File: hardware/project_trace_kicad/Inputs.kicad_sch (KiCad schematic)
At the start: 46 parts, among them J102 Conn_Coaxial, J201 Conn_01x01_Socket, J202 Conn_01x01_Socket, J203 Conn_01x01_Socket, J204 Screw_Terminal_01x04, U101 AD8421, U102 AQW280SX, U201 AQW282SX, U202 DAC81401, U203 TS5A23159DGS, U204 ADA4807-2ACP

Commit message: Before Changes to Input Section
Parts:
- removed DZ201: WE-TVSP, Diode_SMD:D_SMC_Handsoldering, symbol PCM_Diode_Zener_AKL:D_Zener_Generic
- added C303: 100n, Capacitor_SMD:C_0603_1608Metric_Pad1.08x0.95mm_HandSolder, symbol Device:C
- added D201: SMAJ250A, Diode_SMD:D_SMA_Handsoldering, symbol Device:D_Zener_Filled
- added U302: ADA4807-4ARUZ, Package_SO:TSSOP-14_4.4x5mm_P0.65mm, symbol Amplifier_Operational:ADA4807-4ARUZ
- C201, C202, C204, C205, C206, C207: value 1u -> 100n; footprint (none) -> Capacitor_SMD:C_0603_1608Metric_Pad1.08x0.95mm_HandSolder
- C203, C?: footprint (none) -> Capacitor_SMD:C_0603_1608Metric_Pad1.08x0.95mm_HandSolder
- JP201, JP202, JP203, JP204, JP205: footprint (none) -> Jumper:SolderJumper-2_P1.3mm_Open_RoundedPad1.0x1.5mm
- U101: footprint Package_SO:SOIC-8_3.9x4.9mm_P1.27mm -> Package_SO:MSOP-8_3x3mm_P0.65mm; DigikeyPN (none) -> 505-AD8421ARMZ-RLCT-ND
- U203: DigikeyPN (none) -> 296-18598-1-ND
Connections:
- net +5V: now also C303.2, U302.4 (V+)
- net GND: now also DZ?.1 (K), J204.3 (Pin_3), R104.2, C303.1, D201.2 (A), U302.11 (V-); no longer R103.2
- net VCOM: now also R103.2; no longer DZ?.1 (K), J204.3 (Pin_3), R104.2
- net Voltmeter.In: now also D201.1 (K)
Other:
- note added: "1.8Vpp"
- note added: "5Vpp"
- note added: "TODO: Fix high relative uncertainty due to Ron"
- note added: "TODO: UPDATE AD4821 FOOTPRINT"
- note added: "TODO: Verify Footprint"
- note added: "TODO: use GND (Requires changes to R-LADDER)"
- note removed: "TODO: Use Diff-amp?"
- moved on the sheet: C204, R105, R?, U201B, U203C

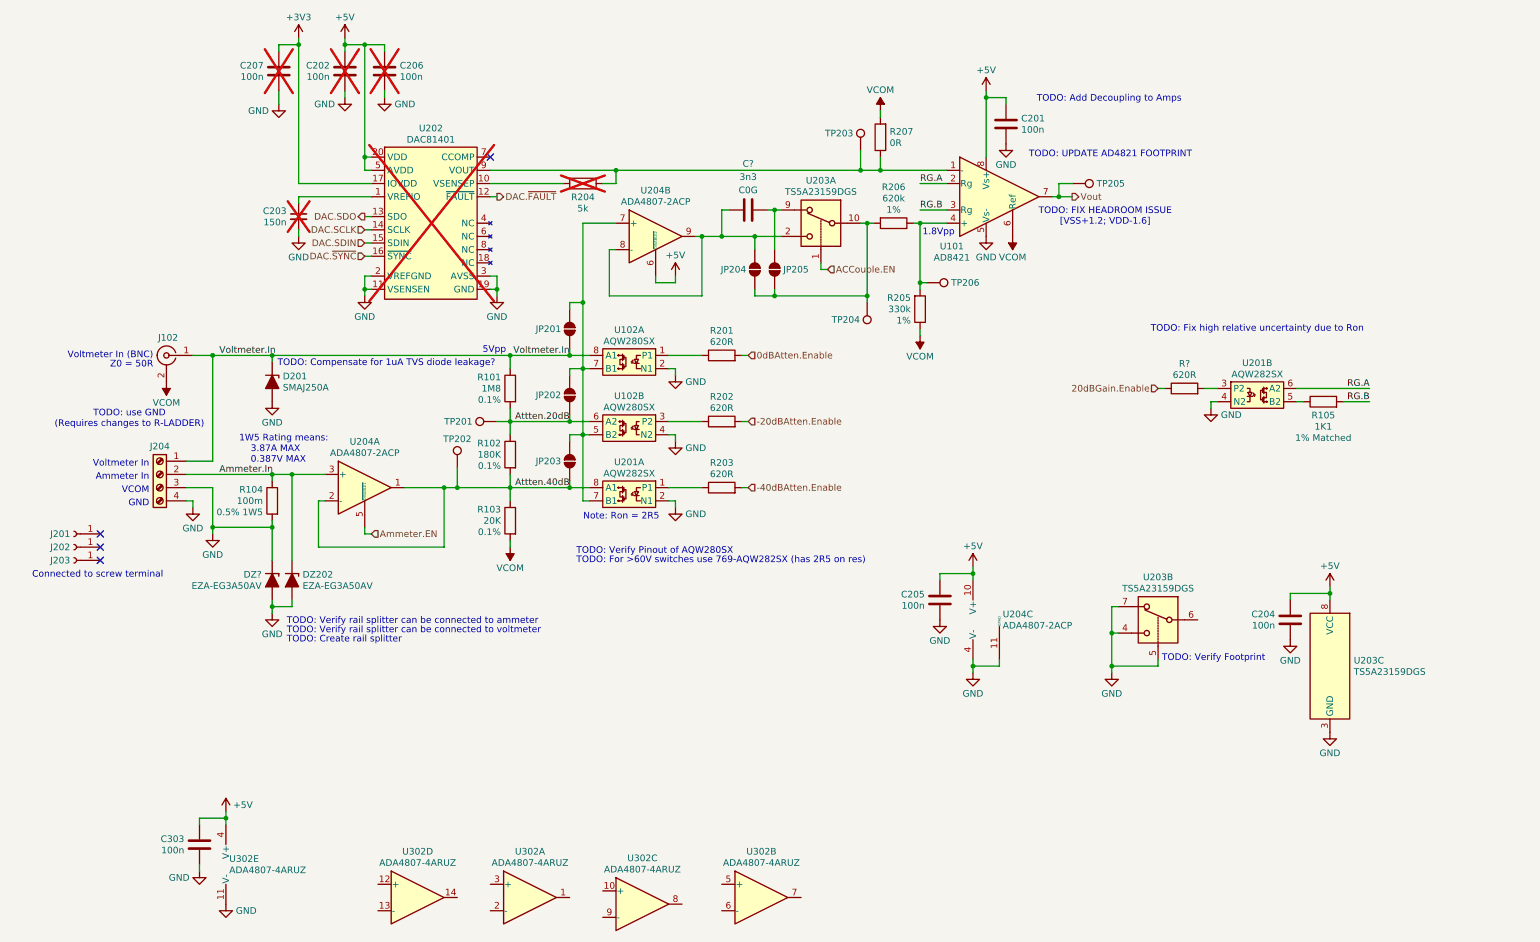
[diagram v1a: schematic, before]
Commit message: Add Pull-Up Network to Input
(Sync up laptop)
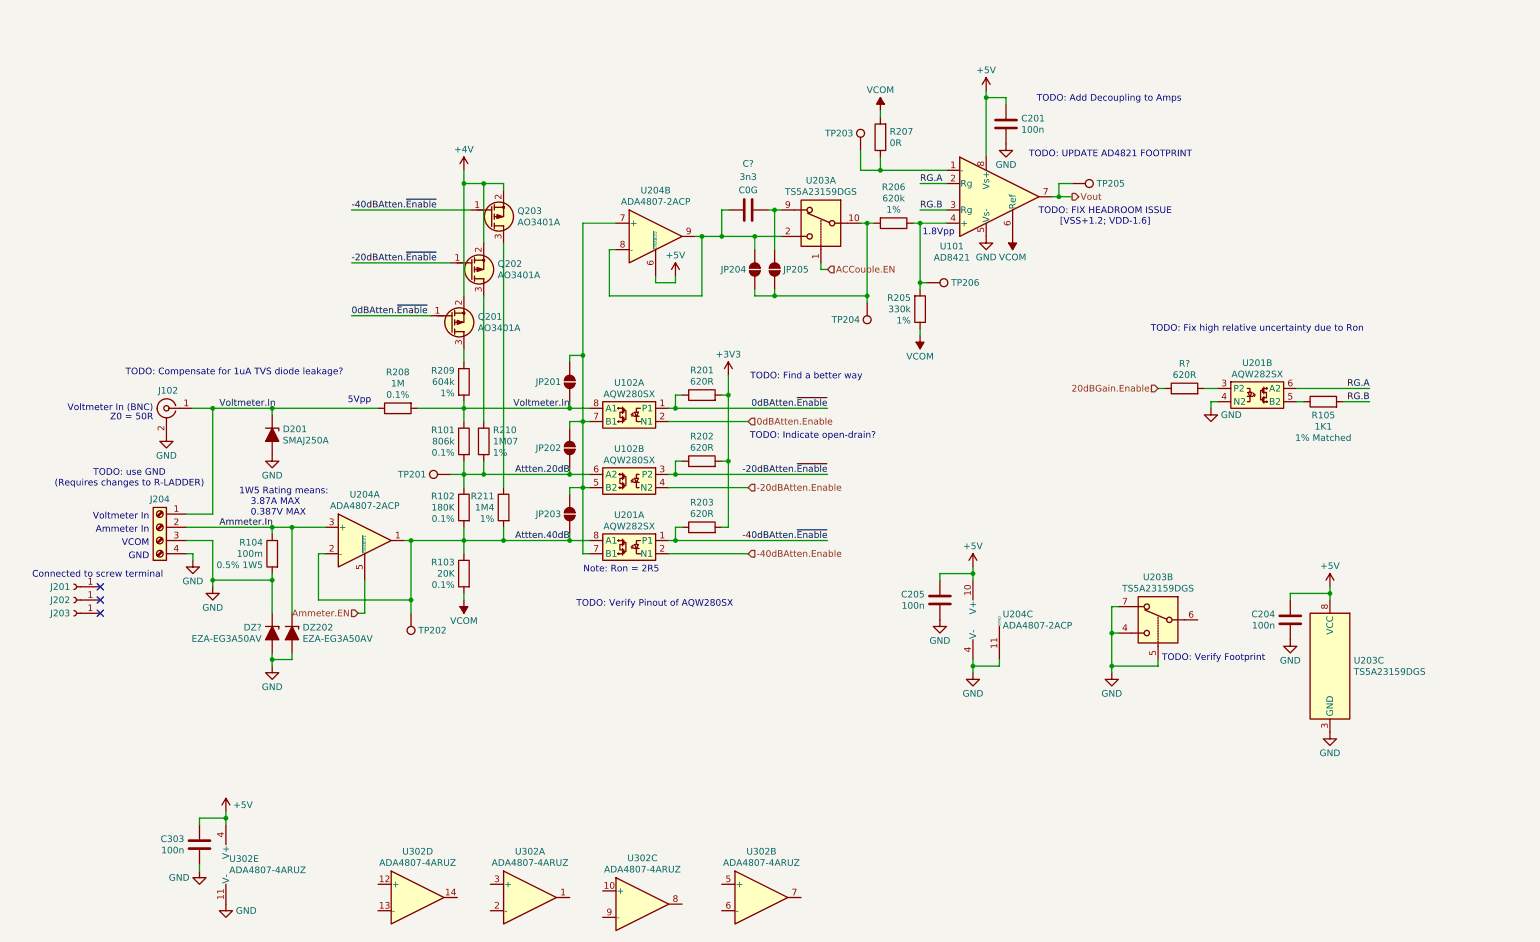
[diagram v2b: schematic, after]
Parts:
- removed C202, C206, C207: 100n, Capacitor_SMD:C_0603_1608Metric_Pad1.08x0.95mm_HandSolder, symbol Device:C
- removed C203: 150n, Capacitor_SMD:C_0603_1608Metric_Pad1.08x0.95mm_HandSolder, symbol Device:C_Small
- removed R204: 5k, symbol Device:R
- removed U202: DAC81401, Package_SO:Texas_PW0020A_TSSOP-20_4.4x6.5mm_P0.65mm, symbol ProjectTraceSymbols:DAC81401
- added Q201, Q202, Q203: AO3401A, PCM_Package_TO_SOT_SMD_AKL:SOT-23, symbol PCM_Transistor_MOSFET_AKL:AO3401A
- added R208: 1M, Resistor_SMD:R_0603_1608Metric_Pad0.98x0.95mm_HandSolder, symbol Device:R
- added R209: 604k, Resistor_SMD:R_0603_1608Metric_Pad0.98x0.95mm_HandSolder, symbol Device:R
- added R210: 1M07, Resistor_SMD:R_0603_1608Metric_Pad0.98x0.95mm_HandSolder, symbol Device:R
- added R211: 1M4, Resistor_SMD:R_0603_1608Metric_Pad0.98x0.95mm_HandSolder, symbol Device:R
- R101: value 1M8 -> 806k
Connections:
- net +3V3: now also R201.2, R202.2, R203.2
- net -20dBAtten.Enable: now also U102.4 (N2); no longer R202.2
- net -40dBAtten.Enable: now also U201.2 (N1); no longer R203.2
- net 0dBAtten.Enable: now also U102.2 (N1); no longer R201.2
- net Attten.20dB: now also R210.2
- net Attten.40dB: now also R211.2
- net GND: now also J102.2 (Ext); no longer U102.2 (N1), U102.4 (N2), U201.2 (N1)
- net VCOM: no longer J102.2 (Ext)
- net Voltmeter.In: now also R208.1, R208.2, R209.2
- net -40dBAtten.~{Enable}: now reaches R203.1, U201.1 (P1)
- net -40dBAtten.~{Enable}: now also Q203.1 (G)
- net 0dBAtten.~{Enable}: now reaches R201.1, U102.1 (P1)
- net 0dBAtten.~{Enable}: now also Q201.1 (G)
- net -20dBAtten.~{Enable}: now reaches R202.1, U102.3 (P2)
- net -20dBAtten.~{Enable}: now also Q202.1 (G)
- new net: Q201.3 (D), R209.1
- new net: Q202.3 (D), R210.1
- new net: Q203.3 (D), R211.1
- new net +4V: Q201.2 (S), Q202.2 (S), Q203.2 (S)
- no-connect marks 4 -> 3
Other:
- note added: "TODO: Find a better way"
- note added: "TODO: Indicate open-drain?"
- note removed: "TODO: Create rail splitter"
- note removed: "TODO: For >60V switches use 769-AQW282SX (has 2R5 on res)"
- note removed: "TODO: Verify rail splitter can be connected to ammeter"
- note removed: "TODO: Verify rail splitter can be connected to voltmeter"
- moved on the sheet: D201, DZ202, DZ?, J102, J201, J202, J203, J204, JP201, JP202, JP203, R101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

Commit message: Change designators, Improve Input Circuit
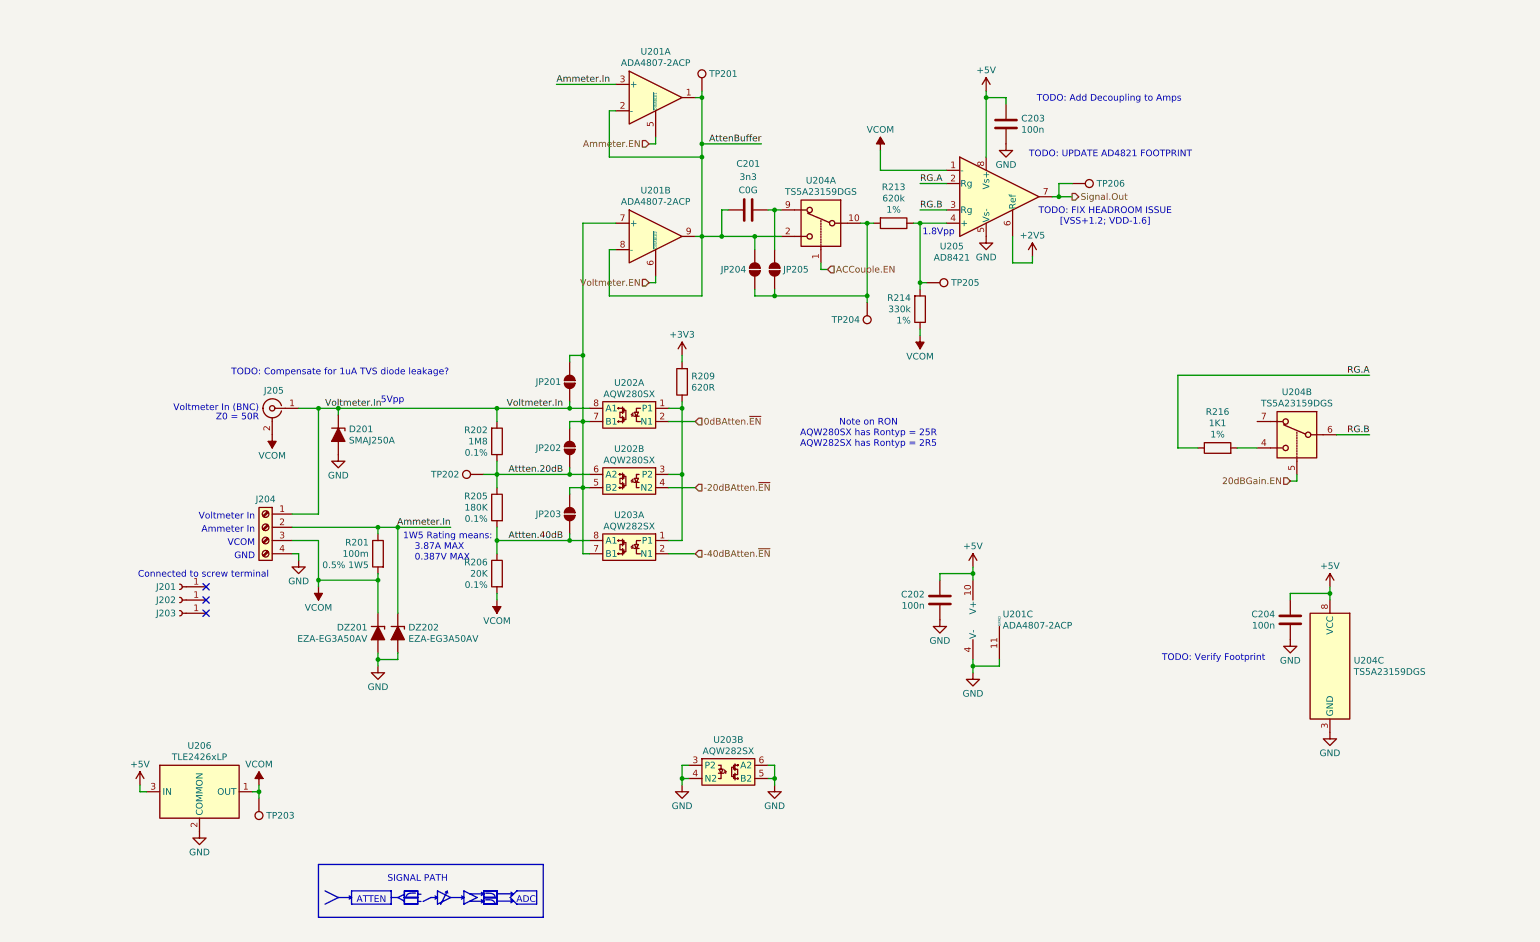
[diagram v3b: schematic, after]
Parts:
- removed C303: 100n, Capacitor_SMD:C_0603_1608Metric_Pad1.08x0.95mm_HandSolder, symbol Device:C
- removed Q201, Q202, Q203: AO3401A, PCM_Package_TO_SOT_SMD_AKL:SOT-23, symbol PCM_Transistor_MOSFET_AKL:AO3401A
- removed R101: 806k, Resistor_SMD:R_0603_1608Metric_Pad0.98x0.95mm_HandSolder, symbol Device:R
- removed R202, R203, R?: 620R, Resistor_SMD:R_0603_1608Metric_Pad0.98x0.95mm_HandSolder, symbol Device:R
- removed R207: 0R, symbol Device:R
- removed R209: 604k, Resistor_SMD:R_0603_1608Metric_Pad0.98x0.95mm_HandSolder, symbol Device:R
- removed R210: 1M07, Resistor_SMD:R_0603_1608Metric_Pad0.98x0.95mm_HandSolder, symbol Device:R
- removed R211: 1M4, Resistor_SMD:R_0603_1608Metric_Pad0.98x0.95mm_HandSolder, symbol Device:R
- removed U302: ADA4807-4ARUZ, Package_SO:TSSOP-14_4.4x5mm_P0.65mm, symbol Amplifier_Operational:ADA4807-4ARUZ
- added U206: TLE2426xLP, Package_TO_SOT_THT:TO-92_Inline_Wide, symbol Reference_Voltage:TLE2426xLP
- R202: renamed from R208; value 1M -> 1M8
- R216: renamed from R105; Extra 1% Matched -> 1%
- gave numbers to parts that had none: 2
- renumbered C205 to C202, C201 to C203, J102 to J205, R104 to R201, R102 to R205, R103 to R206, R201 to R209, R206 to R213, R205 to R214, TP202 to TP201, TP201 to TP202, TP206 to TP205, TP205 to TP206, U204 to U201, U102 to U202, U201 to U203, U203 to U204, U101 to U205
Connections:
- net -40dBAtten.~{Enable} is gone; now on an unnamed net: U203.1 (P1)
- net 0dBAtten.~{Enable} is gone; now on an unnamed net: R209.1, U202.1 (P1)
- net +5V: now also U206.3 (IN); no longer U201.6 (~{DISABLE2})
- net Attten.20dB: now also R202.1
- net Attten.40dB: no longer TP201.1, U201.1, U201.2 (-)
- net GND: now also U203.3 (P2), U203.5 (B2), U203.6 (A2), U206.2 (COMMON); no longer DZ201.1 (K), J204.3 (Pin_3), J205.2 (Ext), R201.2, U204.4, U204.5, U204.7
- net RG.A: now also R216.1; no longer U203.6 (A2)
- net RG.B: now also U204.6; no longer R216.2
- net VCOM: now also DZ201.1 (K), J204.3 (Pin_3), J205.2 (Ext), R201.2, TP203.1, U205.1 (-), U206.1 (OUT); no longer U205.6 (Ref)
- net Voltmeter.In: no longer R202.1
- net AttenBuffer: now reaches C201.1, JP204.1 (A), U201.8 (-), U201.9, U204.2
- net AttenBuffer: now also TP201.1, U201.1, U201.2 (-)
- net -20dBAtten.Enable renamed -20dBAtten.~{EN}
- net -20dBAtten.~{Enable}: no longer names the net of U202.3 (P2)
- net -40dBAtten.Enable renamed -40dBAtten.~{EN}
- net 0dBAtten.Enable renamed 0dBAtten.~{EN}
- net Vout renamed Signal.Out
- new net: R216.2, U204.4
- new net +2V5: U205.6 (Ref)
- new net 20dBGain.EN: U204.5
- new net Voltmeter.EN: U201.6 (~{DISABLE2})
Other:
- note added: "ADC"
- note added: "ATTEN"
- note added: "Note on RON AQW280SX has Rontyp = 25R AQW282SX has Rontyp = 2R5"
- note added: "SIGNAL PATH"
- note removed: "Note: Ron = 2R5"
- note removed: "TODO: Find a better way"
- note removed: "TODO: Fix high relative uncertainty due to Ron"
- note removed: "TODO: Indicate open-drain?"
- note removed: "TODO: Verify Pinout of AQW280SX"
- note removed: "TODO: use GND (Requires changes to R-LADDER)"
- moved on the sheet: D201, DZ201, DZ202, J201, J202, J203, J204, J205, R201, R202, R205, R206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

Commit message: Improve Inputs, Source Parts, Add Credits
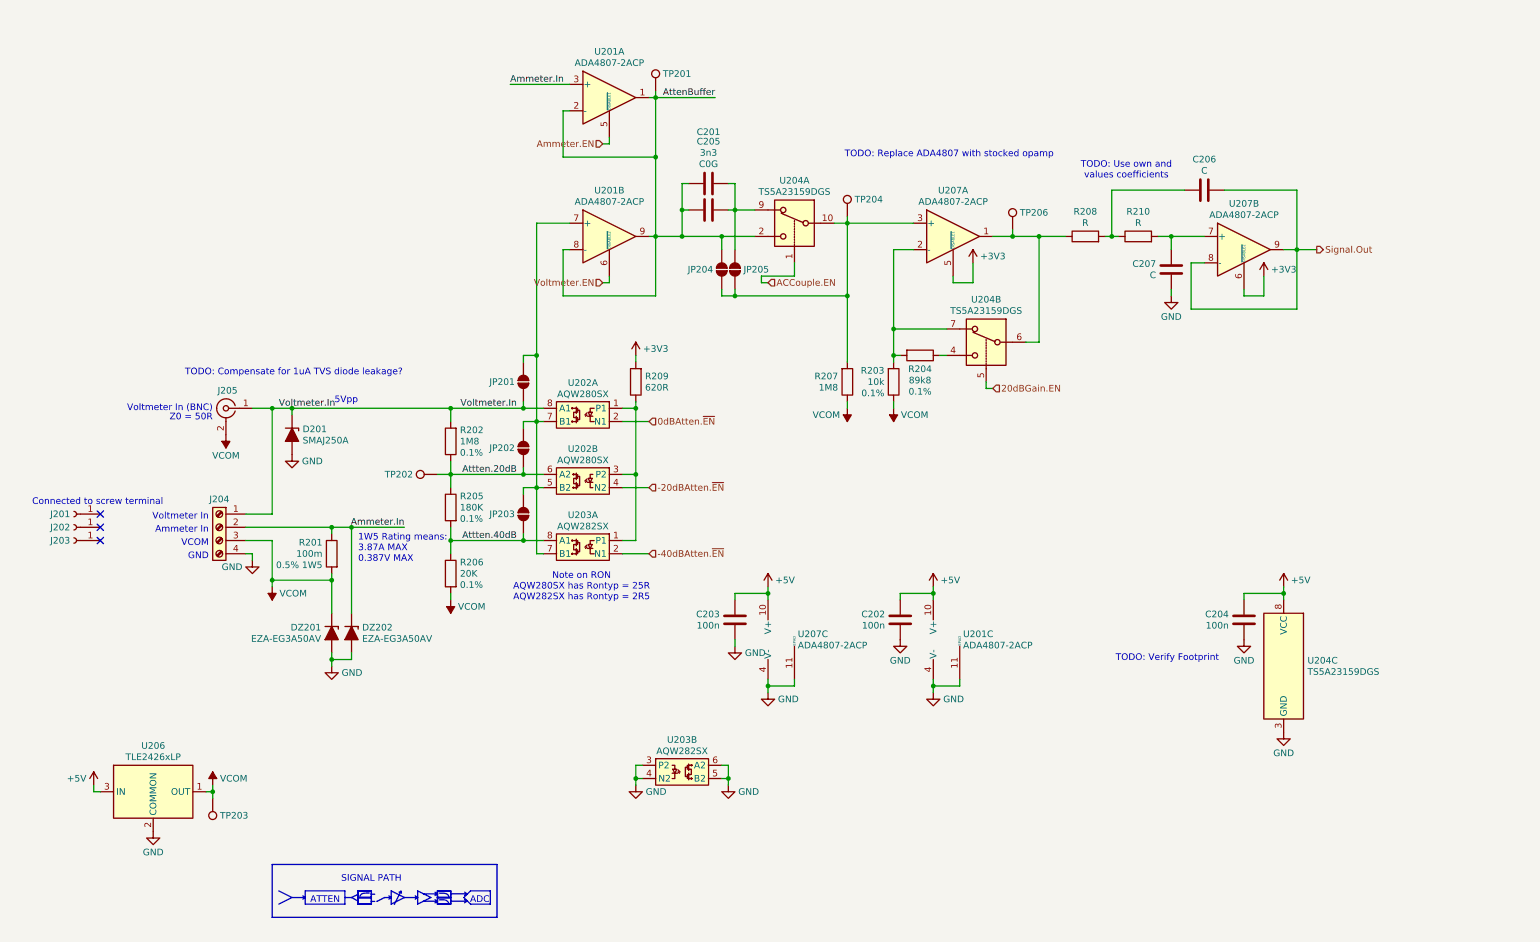
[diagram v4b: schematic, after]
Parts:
- removed R213: 620k, Resistor_SMD:R_0603_1608Metric_Pad0.98x0.95mm_HandSolder, symbol Device:R
- removed R214: 330k, Resistor_SMD:R_0603_1608Metric_Pad0.98x0.95mm_HandSolder, symbol Device:R
- removed R216: 1K1, Resistor_SMD:R_0603_1608Metric_Pad0.98x0.95mm_HandSolder, symbol Device:R
- removed TP205: TestPoint, TestPoint:TestPoint_Pad_1.5x1.5mm, symbol Connector:TestPoint
- removed U205: AD8421, Package_SO:MSOP-8_3x3mm_P0.65mm, symbol Amplifier_Instrumentation:AD8421
- added C205: 3n3, Capacitor_SMD:C_0603_1608Metric_Pad1.08x0.95mm_HandSolder, symbol Device:C
- added C206, C207: C, symbol Device:C
- added R203: 10k, Resistor_SMD:R_0603_1608Metric_Pad0.98x0.95mm_HandSolder, symbol Device:R
- added R204: 89k8, Resistor_SMD:R_0603_1608Metric_Pad0.98x0.95mm_HandSolder, symbol Device:R
- added R207: 1M8, Resistor_SMD:R_0805_2012Metric_Pad1.20x1.40mm_HandSolder, symbol Device:R
- added R208, R210: R, symbol Device:R
- added U207: ADA4807-2ACP, Package_CSP:LFCSP-WD-10-1EP_3x3mm_P0.5mm_EP1.64x2.38mm, symbol Amplifier_Operational:ADA4807-2ACP
- C201: DigikeyPN (none) -> 490-GCM1885C1H332FA16DCT-ND
- C202, C203, C204: DigikeyPN (none) -> 399-C0603C104K3RACTUCT-ND; Extra (none) -> 25V
- JP201, JP202, JP203, JP204, JP205, TP201, TP202, TP203, TP204, TP206: DigikeyPN (none) -> N/A
- R202: footprint Resistor_SMD:R_0603_1608Metric_Pad0.98x0.95mm_HandSolder -> Resistor_SMD:R_0805_2012Metric_Pad1.20x1.40mm_HandSolder; DigikeyPN (none) -> 408-2026-1-ND
- R205: DigikeyPN (none) -> YAG1548CT-ND
- R206: DigikeyPN (none) -> YAG1582CT-ND
- R209: footprint Resistor_SMD:R_0603_1608Metric_Pad0.98x0.95mm_HandSolder -> Resistor_THT:R_Axial_DIN0207_L6.3mm_D2.5mm_P10.16mm_Horizontal; DigikeyPN (none) -> N/A
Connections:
- net +3V3: now also U207.5 (~{DISABLE1}), U207.6 (~{DISABLE2})
- net +5V: now also U207.10 (V+)
- net AttenBuffer: now also C205.1
- net GND: now also C207.1, U207.11 (EPAD), U207.4 (V-)
- net Signal.Out: now also C206.2, U207.8 (-), U207.9; no longer TP206.1
- net VCOM: now also R203.1, R207.1
- net at JP204.2 (B), JP205.2 (B), TP204.1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: now also R207.2, U207.3 (+)
- net at U204.4: now also R204.1
- net at U204.7: now also R203.2, R204.2, U207.2 (-)
- net at C201.2, JP205.1 (A), U204.9: now also C205.2
- net RG.B: no longer names the net of U204.6
- net RG.B: now also TP206.1, R208.1, U207.1
- new net: C206.1, R208.2, R210.1
- new net: C207.2, R210.2, U207.7 (+)
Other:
- note added: "TODO: Replace ADA4807 with stocked opamp"
- note added: "TODO: Use own and values coefficients"
- note removed: "1.8Vpp"
- note removed: "TODO: Add Decoupling to Amps"
- note removed: "TODO: FIX HEADROOM ISSUE [VSS+1.2; VDD-1.6]"
- note removed: "TODO: UPDATE AD4821 FOOTPRINT"
- title: (none) -> Multilloscope - Signal Inputs
- moved on the sheet: C201, C202, C204, D201, DZ201, DZ202, J201, J202, J203, J204, J205, JP201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

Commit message: Lotsa Changes
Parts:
- removed U201, U207: ADA4807-2ACP, Package_CSP:LFCSP-WD-10-1EP_3x3mm_P0.5mm_EP1.64x2.38mm, symbol Amplifier_Operational:ADA4807-2ACP
- added U1, U2: OPA2837IRUNT, symbol ProjectTraceSymbols:OPA2837IRUNT
- U202: footprint (none) -> ProjectTraceFootprints:AQW282SX
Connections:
- net +3V3: now also U2.4, U2.6
- net +5V: now also U1.10, U2.10
- net Ammeter.EN: now also U1.4
- net Ammeter.In: now also U1.3 (+)
- net AttenBuffer: now also U1.1, U1.2 (-), U1.8 (-), U1.9
- net GND: now also U1.5, U2.5
- net Signal.Out: now also U2.8 (-), U2.9
- net Voltmeter.EN: now also U1.6
- net at JP204.2 (B), JP205.2 (B), R207.2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: now also U2.3 (+)
- net at R208.1, TP206.1, U204.6: now also U2.1
- net at R203.2, R204.2, U204.7: now also U2.2 (-)
- net at JP201.2 (B), JP202.2 (B), JP203.2 (B)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: now also U1.7 (+)
- net at C207.2, R210.2: now also U2.7 (+)
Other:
- note removed: "TODO: Compensate for 1uA TVS diode leakage?"
- moved on the sheet: C202, C203, R203, R204, U204B
